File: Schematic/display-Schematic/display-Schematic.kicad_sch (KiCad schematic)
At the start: 36 parts, among them U10 5161AS, U11 5161AS, U12 5161AS, U13 5161AS, U4 MAX7219, U5 12101AR, U6 12101AR, U7 12101AR, U8 12101AR, U9 MAX7219

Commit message: started working on the PCB side of the display part
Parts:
- removed down_, left_, right_, setup_, up_: SW_Push_Dual_x2, symbol Switch:SW_Push_Dual_x2
- added SW1: up, Button_Switch_THT:SW_PUSH_6mm, symbol Switch:SW_Push_Dual_x2
- added SW2, SW3: left, Button_Switch_THT:SW_PUSH_6mm, symbol Switch:SW_Push_Dual_x2
- added SW4: down, Button_Switch_THT:SW_PUSH_6mm, symbol Switch:SW_Push_Dual_x2
- added SW5: setup, Button_Switch_THT:SW_PUSH_6mm, symbol Switch:SW_Push_Dual_x2
- C4, C5: footprint (none) -> Capacitor_THT:C_Rect_L7.2mm_W3.0mm_P5.00mm_FKS2_FKP2_MKS2_MKP2
- D1, D2, D3, D4, D5, D6, D7, D8, D9: footprint (none) -> LED_THT:LED_D5.0mm
- J1: footprint (none) -> Connector_IDC:IDC-Header_2x06_P2.54mm_Vertical
- R1, R10, R2, R3, R5, R6, R7, R8, R9: footprint (none) -> Resistor_THT:R_Axial_DIN0207_L6.3mm_D2.5mm_P10.16mm_Horizontal
- U10, U11, U12, U13: footprint (none) -> CustomFootprintLib:5161AS
- U4, U9: footprint (none) -> Package_DIP:CERDIP-24_W7.62mm_SideBrazed_Socket
- U5, U6, U7, U8: footprint (none) -> CustomFootprintLib:12101AR
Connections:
- net +3.3V: now also SW1.2 (D), SW2.2 (D), SW3.2 (D), SW4.2 (D), SW5.2 (D)
- net at J1.5, R10.2: now also SW5.1 (C)
- net at J1.6, R9.2: now also SW3.1 (C)
- net at J1.7, R8.2: now also SW2.1 (C)
- net at J1.8, R7.2: now also SW1.1 (C)
- net at J1.9, R6.2: now also SW4.1 (C)
- no-connect marks 0 -> 36
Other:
- moved on the sheet: J1

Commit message: USC-C to 5V DC plug added to custom lib
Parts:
- U4, U9: footprint Package_DIP:CERDIP-24_W7.62mm_SideBrazed_Socket -> Package_DIP:DIP-24_W7.62mm
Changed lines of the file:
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@@
 			)
 		)
-		(property "Footprint" "Package_DIP:CERDIP-24_W7.62mm_SideBrazed_Socket"
+		(property "Footprint" "Package_DIP:DIP-24_W7.62mm"
 			(at 69.85 74.93 0)
 			(effects
@@
 			)
 		)
-		(property "Footprint" "Package_DIP:CERDIP-24_W7.62mm_SideBrazed_Socket"
+		(property "Footprint" "Package_DIP:DIP-24_W7.62mm"
 			(at 92.71 118.11 0)
 			(effects

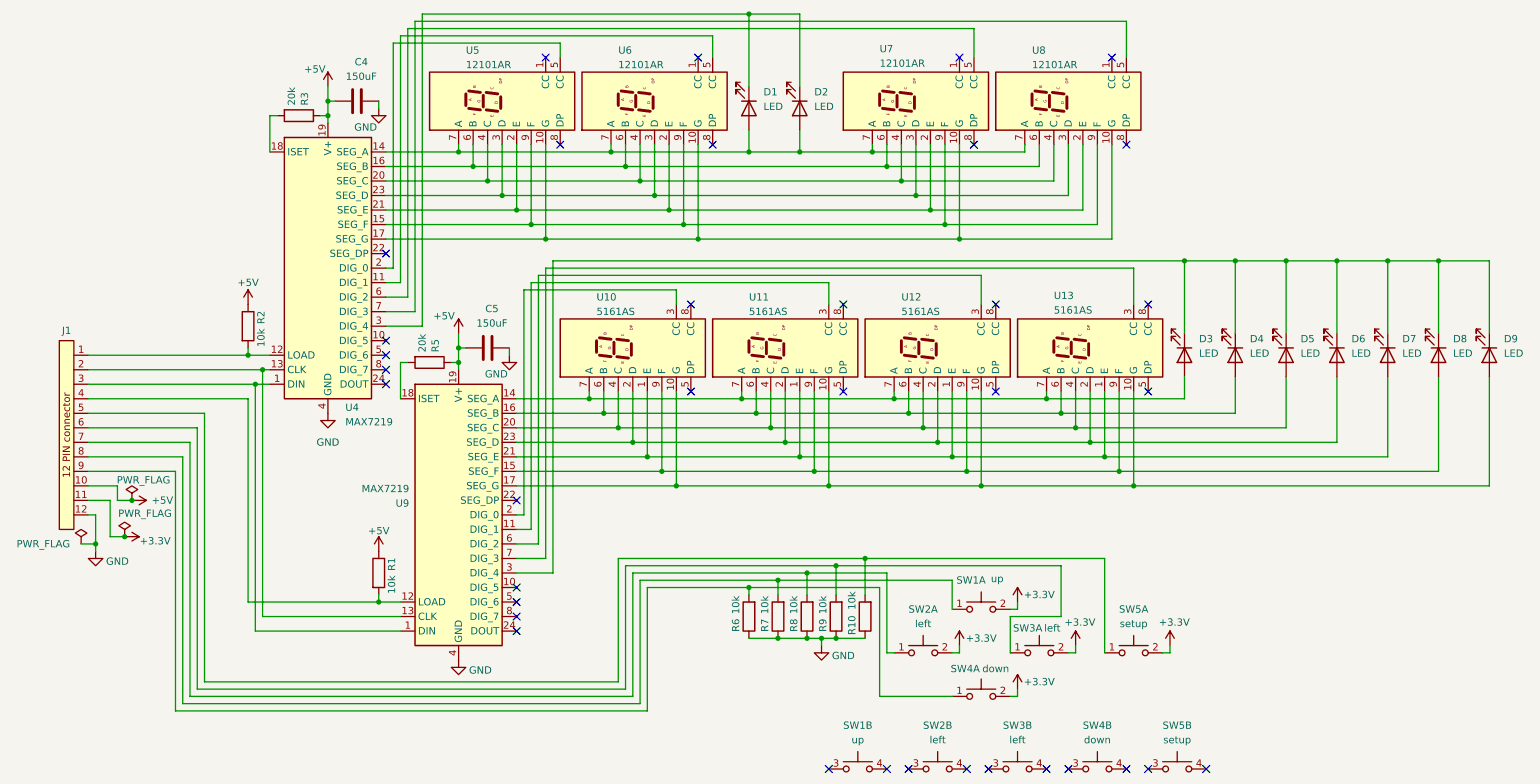
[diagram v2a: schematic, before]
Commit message: Finished the display PCB. A lot of changes went throough to ensure only one layer was used for connections. To change : plug pin placement ; switches are now pull up ; in the code : digit codes are now differents, and differents from display 1 to display 2
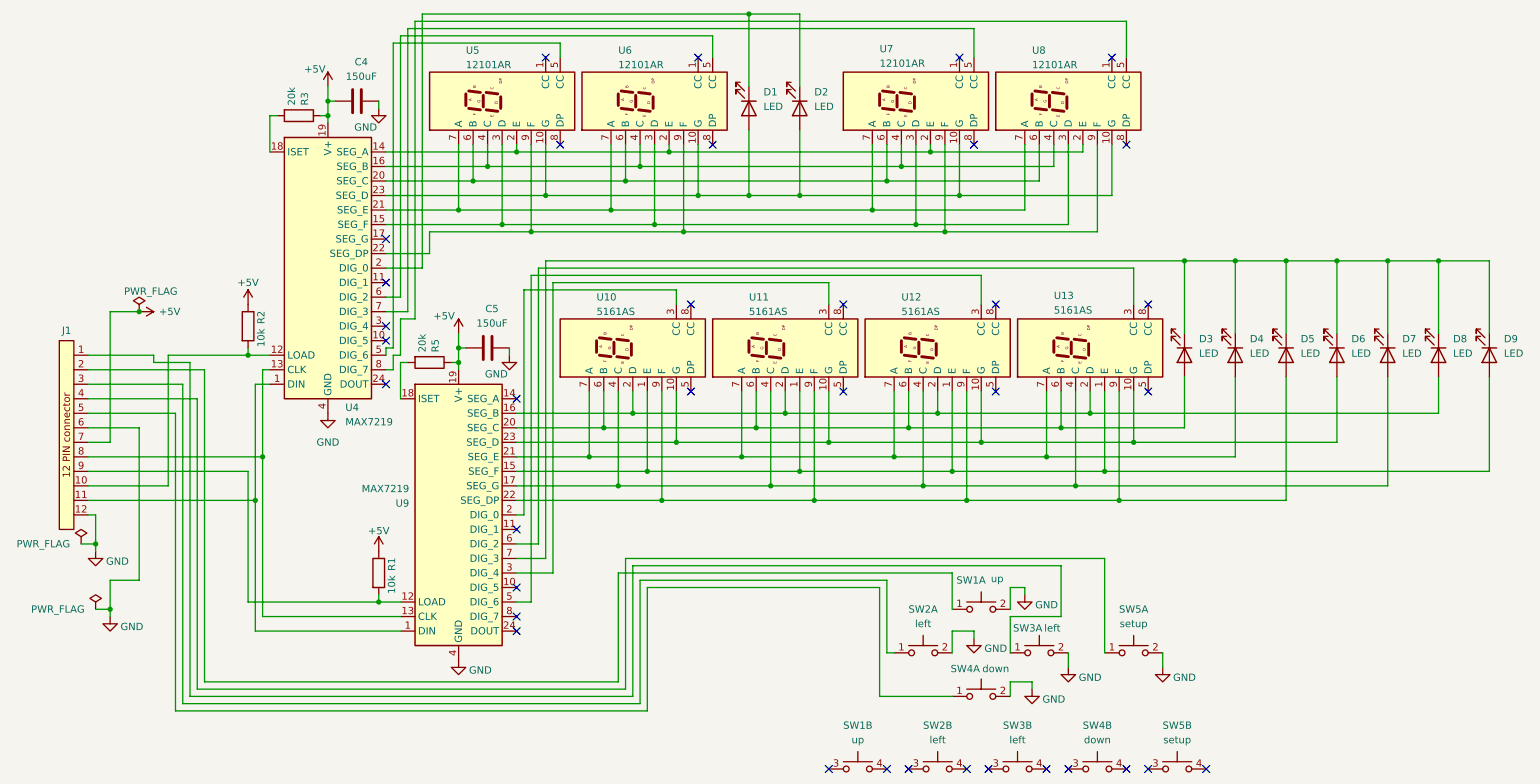
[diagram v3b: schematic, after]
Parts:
- removed R10, R6, R7, R8, R9: 10k, Resistor_THT:R_Axial_DIN0207_L6.3mm_D2.5mm_P10.16mm_Horizontal, symbol Device:R
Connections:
- net +5V: now also J1.7; no longer J1.10
- net GND: now also J1.6, SW1.2 (D), SW2.2 (D), SW3.2 (D), SW4.2 (D), SW5.2 (D)
- net at U10.1 (E), U11.1 (E), U12.1 (E)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: now also D9.2 (A), U9.15 (SEG_F); no longer D7.2 (A), U9.21 (SEG_E)
- net at U10.10 (G), U11.10 (G), U12.10 (G)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: now also D6.2 (A), U9.23 (SEG_D); no longer D9.2 (A), U9.17 (SEG_G)
- net at U10.2 (D), U11.2 (D), U12.2 (D)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: now also D8.2 (A), U9.16 (SEG_B); no longer D6.2 (A), U9.23 (SEG_D)
- net at U13.3 (CC): now also U9.6 (DIG_2); no longer U9.7 (DIG_3)
- net at U10.4 (C), U11.4 (C), U12.4 (C)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: now also D7.2 (A), U9.17 (SEG_G); no longer D5.2 (A), U9.20 (SEG_C)
- net at U10.6 (B), U11.6 (B), U12.6 (B)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: now also D3.2 (A), U9.20 (SEG_C); no longer D4.2 (A), U9.16 (SEG_B)
- net at U10.7 (A), U11.7 (A), U12.7 (A)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: now also D4.2 (A), U9.21 (SEG_E); no longer D3.2 (A), U9.14 (SEG_A)
- net at U10.9 (F), U11.9 (F), U12.9 (F)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: now also D5.2 (A), U9.22 (SEG_DP); no longer D8.2 (A), U9.15 (SEG_F)
- net at SW5.1 (C): now also J1.4; no longer J1.5
- net at D3.1 (K), D4.1 (K), D5.1 (K)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: now also U9.7 (DIG_3); no longer U9.3 (DIG_4)
- net at R2.2, U4.12 (LOAD): now also J1.10; no longer J1.1
- net at U4.13 (CLK), U9.13 (CLK): now also J1.8; no longer J1.2
- net at U4.1 (DIN), U9.1 (DIN): now also J1.11; no longer J1.3
- net at R1.2, U9.12 (LOAD): now also J1.9; no longer J1.4
- net at SW3.1 (C): now also J1.1; no longer J1.6
- net at SW2.1 (C): now also J1.3; no longer J1.7
- net at SW1.1 (C): now also J1.2; no longer J1.8
- net at SW4.1 (C): now also J1.5; no longer J1.9
- net at U12.3 (CC): now also U9.5 (DIG_6); no longer U9.6 (DIG_2)
- net at U5.10 (G), U6.10 (G), U7.10 (G)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: now also D1.2 (A), D2.2 (A), U4.23 (SEG_D); no longer U4.17 (SEG_G)
- net at U5.2 (E), U6.2 (E), U7.2 (E)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: now also U4.14 (SEG_A); no longer U4.21 (SEG_E)
- net at U5.3 (D), U6.3 (D), U7.3 (D)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: now also U4.15 (SEG_F); no longer U4.23 (SEG_D)
- net at U5.4 (C), U6.4 (C), U7.4 (C)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: now also U4.16 (SEG_B); no longer U4.20 (SEG_C)
- net at U6.5 (CC): now also U4.6 (DIG_2); no longer U4.11 (DIG_1)
- net at U5.6 (B), U6.6 (B), U7.6 (B)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: now also U4.20 (SEG_C); no longer U4.16 (SEG_B)
- net at U5.7 (A), U6.7 (A), U7.7 (A)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: now also U4.21 (SEG_E); no longer D1.2 (A), D2.2 (A), U4.14 (SEG_A)
- net at U5.9 (F), U6.9 (F), U7.9 (F)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: now also U4.22 (SEG_DP); no longer U4.15 (SEG_F)
- net at U4.2 (DIG_0): now also D1.1 (K), D2.1 (K); no longer U5.5 (CC)
- net at U4.5 (DIG_6): now also U5.5 (CC)
- net at U7.5 (CC): now also U4.7 (DIG_3); no longer U4.6 (DIG_2)
- net at U8.5 (CC): now also U4.8 (DIG_7); no longer U4.7 (DIG_3)
- net at U11.3 (CC): now also U9.3 (DIG_4); no longer U9.11 (DIG_1)
- removed net +3.3V: J1.11, SW1.2 (D), SW2.2 (D), SW3.2 (D), SW4.2 (D), SW5.2 (D)
- now unconnected: U4.3 (DIG_4)

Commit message: Further work on the hardware side of the pcb
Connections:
- net GND: no longer J1.6, SW1.2 (D), SW2.2 (D), SW3.2 (D), SW4.2 (D), SW5.2 (D)
- new net +3.3V: J1.6, SW1.2 (D), SW2.2 (D), SW3.2 (D), SW4.2 (D), SW5.2 (D)
